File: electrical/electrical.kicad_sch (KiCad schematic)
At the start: 0 parts

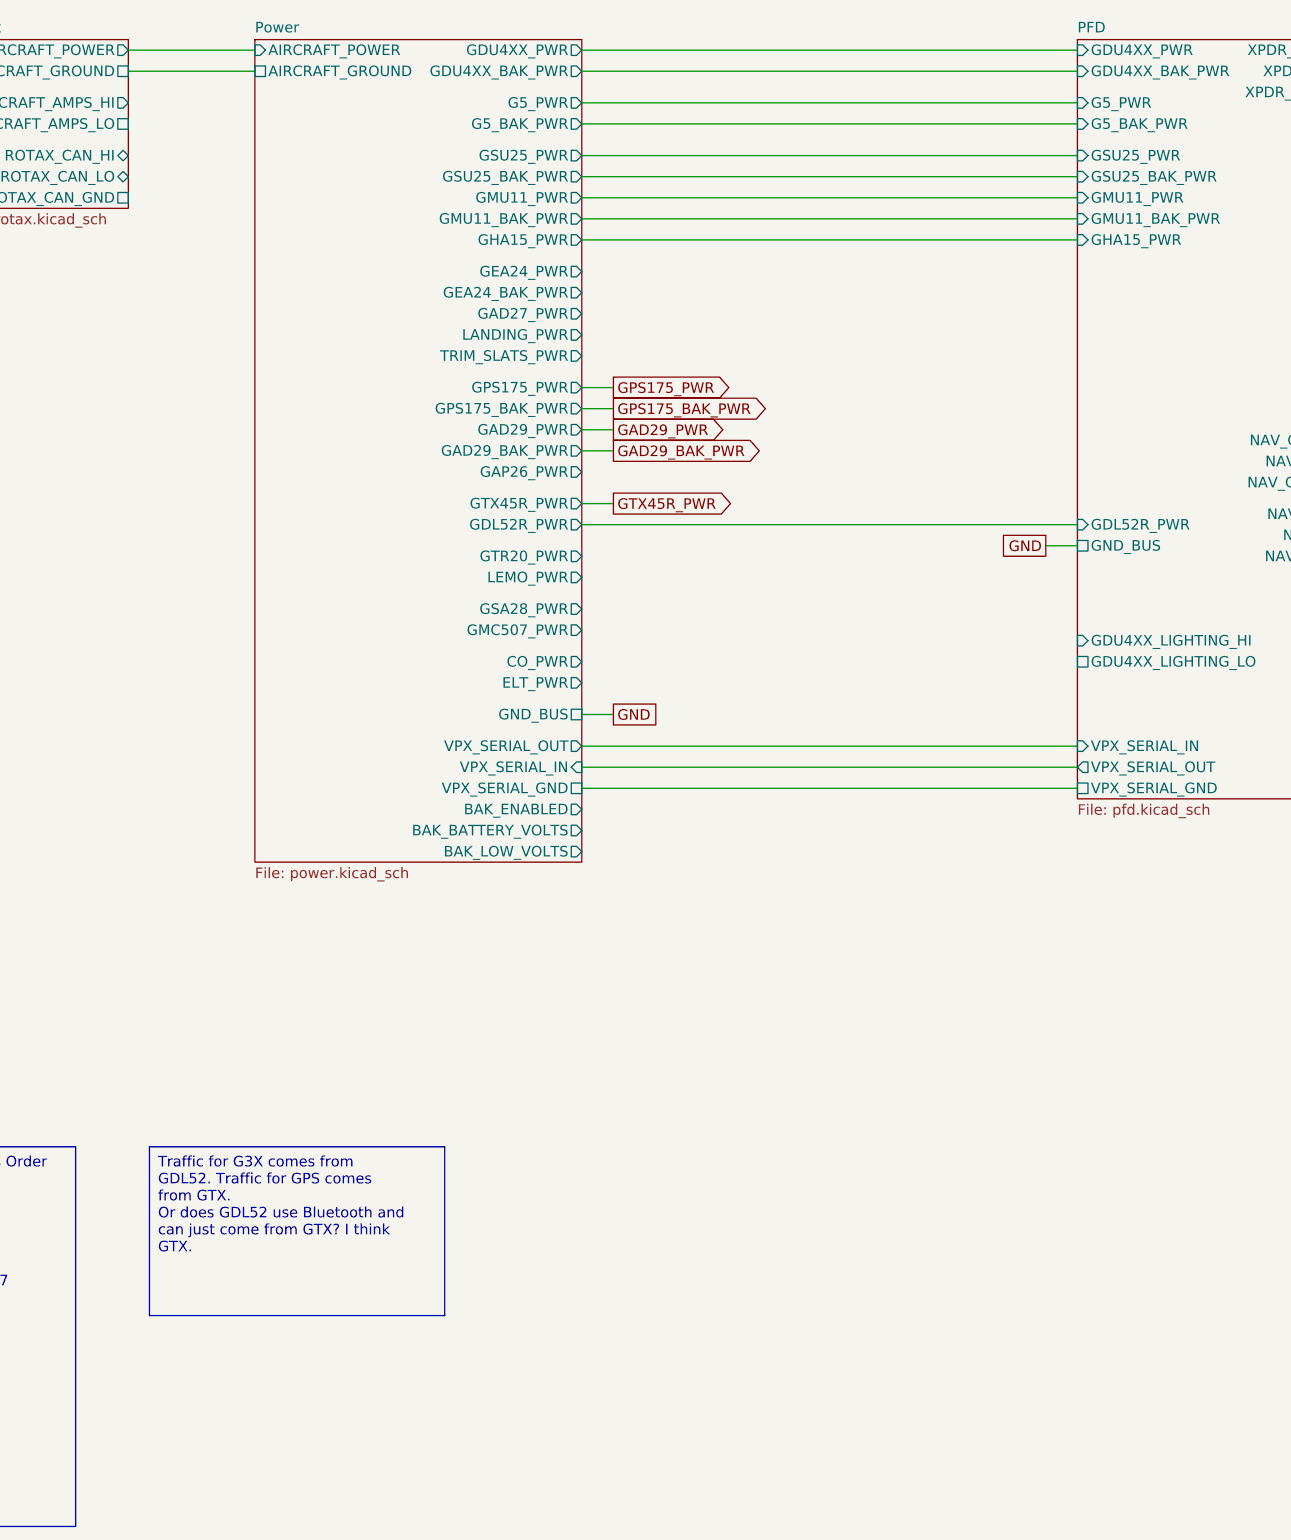
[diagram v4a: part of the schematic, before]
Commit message: Made more grounds passive, added EIS sheet
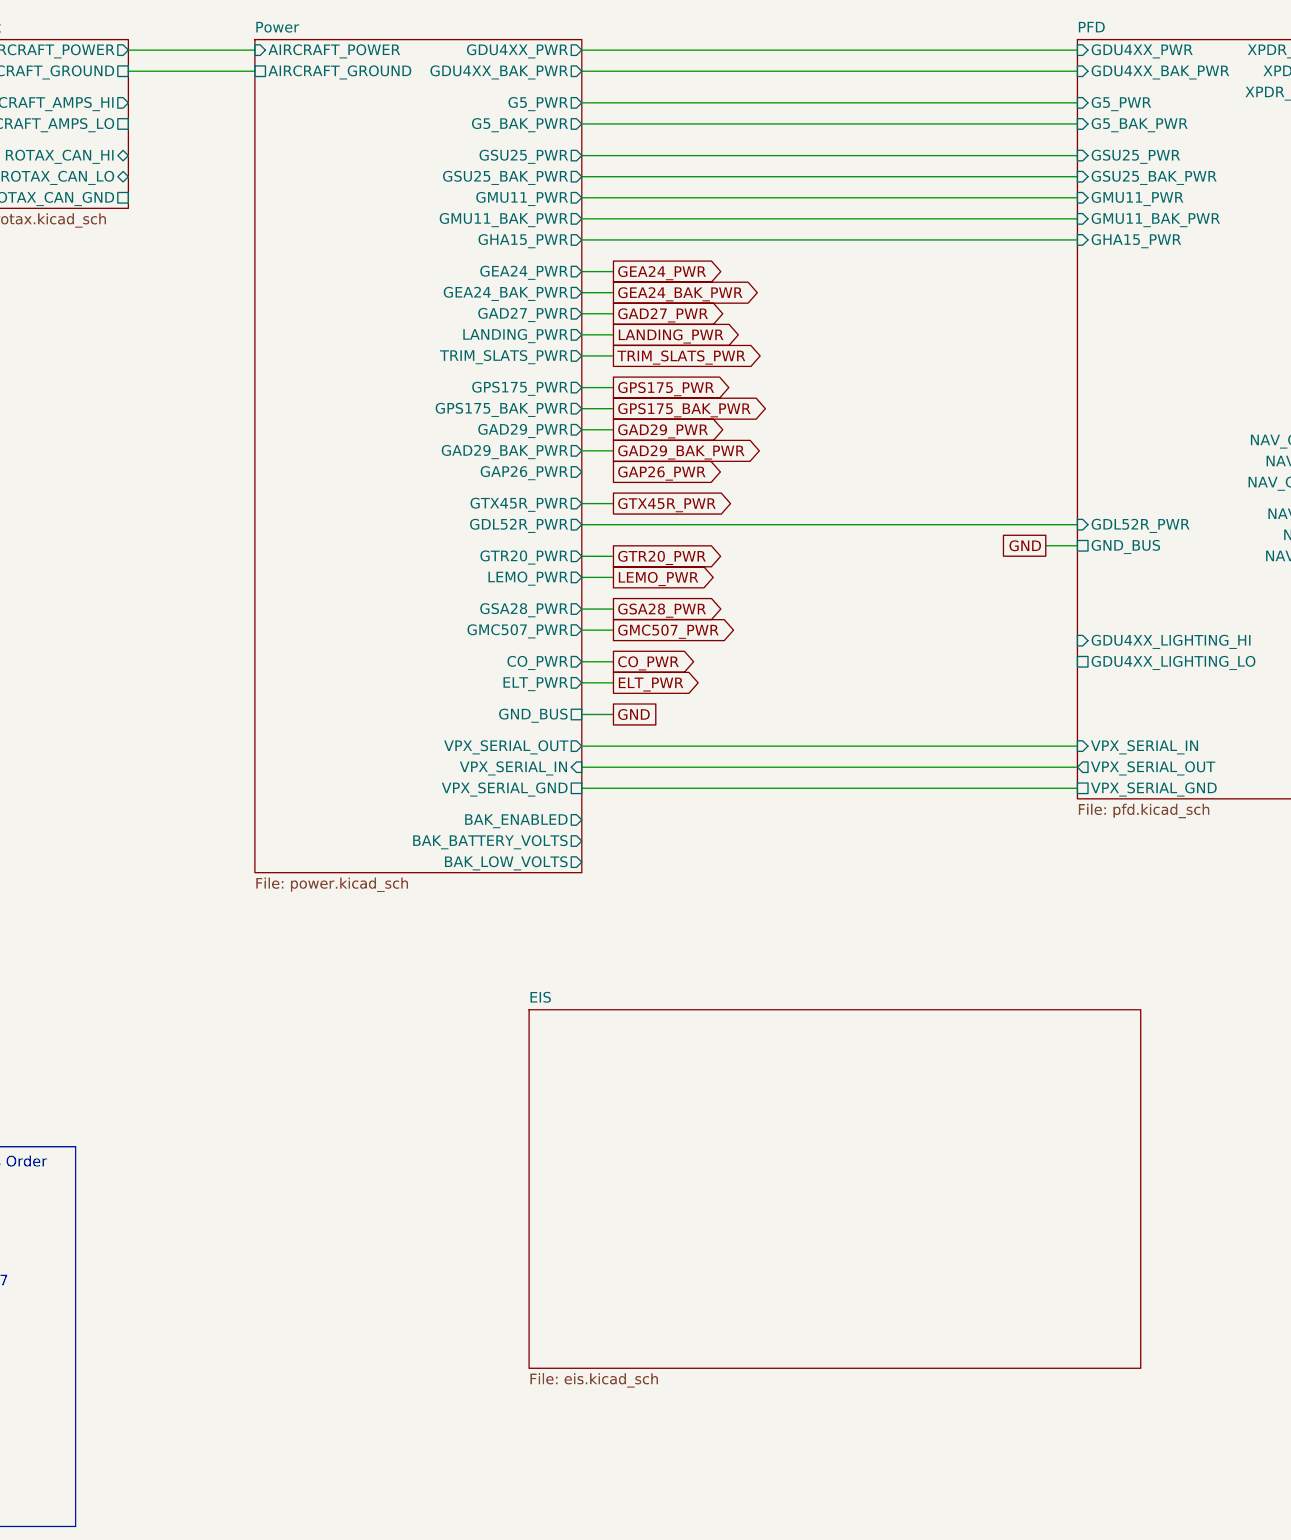
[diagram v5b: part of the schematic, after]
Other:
- added sheet EIS (eis.kicad_sch)
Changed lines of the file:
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@@
+    (stroke (width 0) (type default))
+  )
+  (wire (pts (xy 92.71 100.33) (xy 96.52 100.33))
     (stroke (width 0) (type default))
   )
@@
     (stroke (width 0) (type default))
   )
+  (wire (pts (xy 92.71 106.68) (xy 96.52 106.68))
+    (stroke (width 0) (type default))
+  )
+  (wire (pts (xy 92.71 97.79) (xy 96.52 97.79))
+    (stroke (width 0) (type default))
+  )
   (wire (pts (xy 92.71 76.2) (xy 96.52 76.2))
     (stroke (width 0) (type default))
@@
     (stroke (width 0) (type default))
   )
+  (wire (pts (xy 92.71 57.15) (xy 96.52 57.15))
+    (stroke (width 0) (type default))
+  )
   (wire (pts (xy 92.71 78.74) (xy 96.52 78.74))
     (stroke (width 0) (type default))
@@
     (stroke (width 0) (type default))
   )
+  (wire (pts (xy 92.71 104.14) (xy 96.52 104.14))
+    (stroke (width 0) (type default))
+  )
+  (wire (pts (xy 92.71 59.69) (xy 96.52 59.69))
+    (stroke (width 0) (type default))
+  )
   (wire (pts (xy 199.39 77.47) (xy 262.89 77.47))
     (stroke (width 0) (type default))
@@
     (stroke (width 0) (type default))
   )
+  (wire (pts (xy 92.71 67.31) (xy 96.52 67.31))
+    (stroke (width 0) (type default))
+  )
   (wire (pts (xy 199.39 88.9) (xy 262.89 88.9))
     (stroke (width 0) (type default))
@@
     (stroke (width 0) (type default))
   )
+  (wire (pts (xy 92.71 64.77) (xy 96.52 64.77))
+    (stroke (width 0) (type default))
+  )
   (wire (pts (xy 262.89 53.34) (xy 251.46 53.34))
     (stroke (width 0) (type default))
@@
     (stroke (width 0) (type default))
   )
+  (wire (pts (xy 92.71 62.23) (xy 96.52 62.23))
+    (stroke (width 0) (type default))
+  )
   (wire (pts (xy 262.89 48.26) (xy 246.38 48.26))
     (stroke (width 0) (type default))
@@
     (stroke (width 0) (type default))
   )
+  (wire (pts (xy 92.71 91.44) (xy 96.52 91.44))
+    (stroke (width 0) (type default))
+  )
   (wire (pts (xy 262.89 55.88) (xy 254 55.88))
     (stroke (width 0) (type default))
@@
     (stroke (width 0) (type default))
   )
+  (wire (pts (xy 92.71 93.98) (xy 96.52 93.98))
+    (stroke (width 0) (type default))
+  )
   (wire (pts (xy 262.89 50.8) (xy 248.92 50.8))
     (stroke (width 0) (type default))
@@
     (stroke (width 0) (type default))
   )
-  (text_box "Traffic for G3X comes from GDL52. Traffic for GPS comes from GTX.\nOr does GDL52 use Bluetooth and can just come from GTX? I think GTX."
-    (at 40.64 162.56 0) (size 35.56 20.32)
+  (text_box "Canbus Order\nGMU11\nGSU25\nG3X\nG5\nGEA24\nGAD27\nGMC507\nGHA15\n"
+    (at 15.24 162.56 0) (size 16.51 45.72)
     (stroke (width 0) (type default))
     (fill (type none))
     (effects (font (size 1.27 1.27)) (justify left top))
   )
-  (text_box "Canbus Order\nGMU11\nGSU25\nG3X\nG5\nGEA24\nGAD27\nGMC507\nGHA15\n"
-    (at 15.24 162.56 0) (size 16.51 45.72)
-    (stroke (width 0) (type default))
-    (fill (type none))
-    (effects (font (size 1.27 1.27)) (justify left top))
-  )
   (global_label "GAD29_PWR" (shape output) (at 96.52 76.2 0) (fields_autoplaced)
     (effects (font (size 1.27 1.27)) (justify left))
@@
     )
   )
+  (global_label "ELT_PWR" (shape output) (at 96.52 106.68 0) (fields_autoplaced)
+    (effects (font (size 1.27 1.27)) (justify left))
+    (property "Intersheetrefs" "${INTERSHEET_REFS}" (at 107.6089 106.68 0)
+      (effects (font (size 1.27 1.27)) (justify left) hide)
+    )
+  )
+  (global_label "TRIM_SLATS_PWR" (shape output) (at 96.52 67.31 0) (fields_autoplaced)
+    (effects (font (size 1.27 1.27)) (justify left))
+    (property "Intersheetrefs" "${INTERSHEET_REFS}" (at 115.2289 67.31 0)
+      (effects (font (size 1.27 1.27)) (justify left) hide)
+    )
+  )
   (global_label "GAD29_PWR" (shape input) (at 320.04 72.39 0) (fields_autoplaced)
     (effects (font (size 1.27 1.27)) (justify left))
@@
     )
   )
+  (global_label "LANDING_PWR" (shape output) (at 96.52 64.77 0) (fields_autoplaced)
+    (effects (font (size 1.27 1.27)) (justify left))
+    (property "Intersheetrefs" "${INTERSHEET_REFS}" (at 112.3867 64.77 0)
+      (effects (font (size 1.27 1.27)) (justify left) hide)
+    )
+  )
   (global_label "GND" (shape passive) (at 96.52 110.49 0) (fields_autoplaced)
     (effects (font (size 1.27 1.27)) (justify left))
@@
     )
   )
+  (global_label "GSA28_PWR" (shape output) (at 96.52 97.79 0) (fields_autoplaced)
+    (effects (font (size 1.27 1.27)) (justify left))
+    (property "Intersheetrefs" "${INTERSHEET_REFS}" (at 110.4513 97.79 0)
+      (effects (font (size 1.27 1.27)) (justify left) hide)
+    )
+  )
+  (global_label "GEA24_PWR" (shape output) (at 96.52 57.15 0) (fields_autoplaced)
+    (effects (font (size 1.27 1.27)) (justify left))
+    (property "Intersheetrefs" "${INTERSHEET_REFS}" (at 110.3908 57.15 0)
+      (effects (font (size 1.27 1.27)) (justify left) hide)
+    )
+  )
   (global_label "GTX45R_PWR" (shape input) (at 320.04 30.48 0) (fields_autoplaced)
     (effects (font (size 1.27 1.27)) (justify left))
     (property "Intersheetrefs" "${INTERSHEET_REFS}" (at 335.1203 30.48 0)
+      (effects (font (size 1.27 1.27)) (justify left) hide)
+    )
+  )
+  (global_label "GAD27_PWR" (shape output) (at 96.52 62.23 0) (fields_autoplaced)
+    (effects (font (size 1.27 1.27)) (justify left))
+    (property "Intersheetrefs" "${INTERSHEET_REFS}" (at 110.5118 62.23 0)
+      (effects (font (size 1.27 1.27)) (justify left) hide)
+    )
+  )
+  (global_label "LEMO_PWR" (shape output) (at 96.52 93.98 0) (fields_autoplaced)
+    (effects (font (size 1.27 1.27)) (justify left))
+    (property "Intersheetrefs" "${INTERSHEET_REFS}" (at 109.4232 93.98 0)
       (effects (font (size 1.27 1.27)) (justify left) hide)
     )
@@
     )
   )
+  (global_label "GTR20_PWR" (shape output) (at 96.52 91.44 0) (fields_autoplaced)
+    (effects (font (size 1.27 1.27)) (justify left))
+    (property "Intersheetrefs" "${INTERSHEET_REFS}" (at 110.3908 91.44 0)
+      (effects (font (size 1.27 1.27)) (justify left) hide)
+    )
+  )
   (global_label "GPS175_PWR" (shape output) (at 96.52 71.12 0) (fields_autoplaced)
     (effects (font (size 1.27 1.27)) (justify left))
@@
     )
   )
+  (global_label "CO_PWR" (shape output) (at 96.52 104.14 0) (fields_autoplaced)
+    (effects (font (size 1.27 1.27)) (justify left))
+    (property "Intersheetrefs" "${INTERSHEET_REFS}" (at 107.0647 104.14 0)
+      (effects (font (size 1.27 1.27)) (justify left) hide)
+    )
+  )
   (global_label "GTX45R_PWR" (shape output) (at 96.52 85.09 0) (fields_autoplaced)
     (effects (font (size 1.27 1.27)) (justify left))
@@
     )
   )
+  (global_label "GEA24_BAK_PWR" (shape output) (at 96.52 59.69 0) (fields_autoplaced)
+    (effects (font (size 1.27 1.27)) (justify left))
+    (property "Intersheetrefs" "${INTERSHEET_REFS}" (at 114.987 59.69 0)
+      (effects (font (size 1.27 1.27)) (justify left) hide)
+    )
+  )
+  (global_label "GAP26_PWR" (shape output) (at 96.52 81.28 0) (fields_autoplaced)
+    (effects (font (size 1.27 1.27)) (justify left))
+    (property "Intersheetrefs" "${INTERSHEET_REFS}" (at 110.5118 81.28 0)
+      (effects (font (size 1.27 1.27)) (justify left) hide)
+    )
+  )
+  (global_label "GMC507_PWR" (shape output) (at 96.52 100.33 0) (fields_autoplaced)
+    (effects (font (size 1.27 1.27)) (justify left))
+    (property "Intersheetrefs" "${INTERSHEET_REFS}" (at 112.0841 100.33 0)
+      (effects (font (size 1.27 1.27)) (justify left) hide)
+    )
+  )
   (global_label "GAD29_BAK_PWR" (shape input) (at 320.04 74.93 0) (fields_autoplaced)
     (effects (font (size 1.27 1.27)) (justify left))
@@
     )
   )
-  (sheet (at 53.34 29.21) (size 39.37 99.06) (fields_autoplaced)
+  (sheet (at 53.34 29.21) (size 39.37 100.33) (fields_autoplaced)
     (stroke (width 0.1524) (type solid))
     (fill (color 0 0 0 0.0000))
@@
       (effects (font (size 1.27 1.27)) (justify left bottom))
     )
-    (property "Sheetfile" "power.kicad_sch" (at 53.34 128.8546 0)
+    (property "Sheetfile" "power.kicad_sch" (at 53.34 130.1246 0)
       (effects (font (size 1.27 1.27)) (justify left top))
     )
@@
       (effects (font (size 1.27 1.27)) (justify right))
     )
-    (pin "BAK_BATTERY_VOLTS" output (at 92.71 124.46 0)
-      (effects (font (size 1.27 1.27)) (justify right))
-    )
-    (pin "BAK_ENABLED" output (at 92.71 121.92 0)
-      (effects (font (size 1.27 1.27)) (justify right))
-    )
-    (pin "BAK_LOW_VOLTS" output (at 92.71 127 0)
+    (pin "BAK_BATTERY_VOLTS" output (at 92.71 125.73 0)
+      (effects (font (size 1.27 1.27)) (justify right))
+    )
+    (pin "BAK_ENABLED" output (at 92.71 123.19 0)
+      (effects (font (size 1.27 1.27)) (justify right))
+    )
+    (pin "BAK_LOW_VOLTS" output (at 92.71 128.27 0)
       (effects (font (size 1.27 1.27)) (justify right))
     )
@@
       )
     )
+  )
+  (sheet (at 86.36 146.05) (size 73.66 43.18) (fields_autoplaced)
+    (stroke (width 0.1524) (type solid))
+    (fill (color 0 0 0 0.0000))
+    (property "Sheetname" "EIS" (at 86.36 145.3384 0)
+      (effects (font (size 1.27 1.27)) (justify left bottom))
+    )
+    (property "Sheetfile" "eis.kicad_sch" (at 86.36 189.8146 0)
+      (effects (font (size 1.27 1.27)) (justify left top))
+    )
+    (instances
+      (project "electrical"
+        (path "/e8ec215a-dbe2-4eba-a577-e50a0a128049" (page "5"))
+      )
+    )

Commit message: Added EIS
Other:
- sheet EIS ports: added AIRCRAFT_AMPS_HI, AIRCRAFT_AMPS_LO, BAK_BATTERY_VOLTS, BAK_ENABLED, BAK_LOW_VOLTS, CAN_HI_IN, CAN_HI_OUT, CAN_LOW_IN, CAN_LO_OUT, GEA24_BAK_PWR, GEA24_PWR, GND_BUS, ROTAX_CAN_HI, ROTAX_CAN_LO; removed none
- sheet Power ports: added none; removed CO_PWR
- sheet Rotax ports: added none; removed ROTAX_CAN_GND

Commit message: Added Multifunction
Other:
- added sheet Multifunction (multifunction.kicad_sch)
- sheet Power ports: added TRIM_FLAPS_PWR; removed TRIM_SLATS_PWR
